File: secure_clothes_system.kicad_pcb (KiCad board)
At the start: 2 copper layers, 0 parts

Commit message: Made the first version of the layout with the ESP32-C3
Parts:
- added AE1: PCB_Antenna_Shield, RF_Antenna:PCB_ANTENNA_2,4GHz_50Ohm, F.Cu at (146.9, 76.0)
- added BT1: Battery_Cell, Connector_PinHeader_2.00mm:PinHeader_1x02_P2.00mm_Vertical, F.Cu at (156.0, 100.5)
- added C1: 4.7uF, Capacitor_SMD:C_0603_1608Metric, F.Cu at (152.7, 102.2)
- added C10: 0.1uF, Capacitor_SMD:C_0402_1005Metric, F.Cu at (151.5, 81.9)
- added C11: 10uF, Capacitor_SMD:C_0805_2012Metric, F.Cu at (143.7, 81.8)
- added C12: 0.1uF, Capacitor_SMD:C_0402_1005Metric, F.Cu at (144.8, 83.8)
- added C13: 1uF, Capacitor_SMD:C_0603_1608Metric, F.Cu at (146.9, 84.1)
- added C14: 1uF, Capacitor_SMD:C_0603_1608Metric, F.Cu at (142.9, 100.0)
- added C15: 1uF, Capacitor_SMD:C_0603_1608Metric, B.Cu at (152.7, 91.5)
- added C16: 1uF, Capacitor_SMD:C_0603_1608Metric, F.Cu at (142.9, 90.2)
- added C2: 10uF, Capacitor_SMD:C_0805_2012Metric, F.Cu at (151.9, 96.5)
- added C3: 1.5pF, Capacitor_SMD:C_0201_0603Metric, F.Cu at (147.1, 81.2)
- added C4: 6pF, Capacitor_SMD:C_0603_1608Metric, F.Cu at (159.2, 83.0)
- added C5: 6pF, Capacitor_SMD:C_0603_1608Metric, F.Cu at (155.2, 78.9)
- added C6: 1.5pF, Capacitor_SMD:C_0201_0603Metric, F.Cu at (149.3, 82.4)
- added C7: 1uF, Capacitor_SMD:C_0603_1608Metric, F.Cu at (153.2, 91.5)
- added C8: 10nF, Capacitor_SMD:C_0603_1608Metric, F.Cu at (146.7, 89.9)
- added C9: 0.1uF, Capacitor_SMD:C_0402_1005Metric, F.Cu at (151.5, 80.9)
- added J1: UART0, Connector_PinHeader_2.00mm:PinHeader_1x04_P2.00mm_Vertical, F.Cu at (163.1, 85.9)
- added L1: 2.2uH, Inductor_SMD:L_Murata_DFE201610P, F.Cu at (149.0, 96.4)
- added L2: 2.5nH, Inductor_SMD:L_0201_0603Metric, F.Cu at (148.2, 81.8)
- added L3: 2nH, Inductor_SMD:L_0201_0603Metric, F.Cu at (146.5, 82.9)
- added R1: 267K, Resistor_SMD:R_0603_1608Metric, F.Cu at (149.7, 102.2)
- added R2: 22, Resistor_SMD:R_0603_1608Metric, F.Cu at (154.1, 82.5)
- added R3: 10k, Resistor_SMD:R_0603_1608Metric, F.Cu at (142.9, 97.0)
- added R4: 10k, Resistor_SMD:R_0603_1608Metric, F.Cu at (142.9, 87.2)
- added SW1: BOOT, Button_Switch_THT:SW_PUSH_1P1T_6x3.5mm_H5.0_APEM_MJTP1250, F.Cu at (140.1, 95.3)
- added SW2: RST, Button_Switch_THT:SW_PUSH_1P1T_6x3.5mm_H5.0_APEM_MJTP1250, F.Cu at (140.1, 85.5)
- added U1: TPS62842DGRR, Package_SO:HVSSOP-8-1EP_3x3mm_P0.65mm_EP1.57x1.89mm_ThermalVias, F.Cu at (151.1, 99.6)
- added U2: ESP32-C3, Package_DFN_QFN:QFN-32-1EP_5x5mm_P0.5mm_EP3.45x3.45mm, F.Cu at (150.7, 87.0)
- added U3: W25X40CLSN, Package_SO:SOIC-8_3.9x4.9mm_P1.27mm, B.Cu at (157.2, 92.7)
- added Y1: 40MHz, Crystal:Crystal_SMD_3225-4Pin_3.2x2.5mm, F.Cu at (157.2, 80.9)
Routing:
- net /ESP32-C3/BOOT: track 0.00 -> 16.4 mm
- net +3V3: track 0.00 -> 13.2 mm
- net /ESP32-C3/U0RXD: track 0.00 -> 12.5 mm
- net /ESP32-C3/U0TXD: track 0.00 -> 12.2 mm
- net /ESP32-C3/CHIP_EN: track 0.00 -> 11.7 mm
- net /ESP32-C3/XTAL_N: track 0.00 -> 10.3 mm
- net /ESP32-C3/VDD3P3: track 0.00 -> 4.93 mm
- net Net-(C5-Pad2): track 0.00 -> 3.53 mm
- net /ESP32-C3/XTAL_P: track 0.00 -> 2.24 mm
- added copper zone on F.Cu, net GND
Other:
- board outline added: 28 x 33.9 mm
- copper layers 2 -> 4

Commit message: Made some fixes with the layout
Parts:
- C1, C13, C14, C15, C16, C4, C5, C7, C8: footprint Capacitor_SMD:C_0603_1608Metric -> Capacitor_SMD:C_0402_1005Metric
- C11, C2: footprint Capacitor_SMD:C_0805_2012Metric -> Capacitor_SMD:C_0402_1005Metric
- R1: value 267K -> 52.3K; footprint Resistor_SMD:R_0603_1608Metric -> Resistor_SMD:R_0402_1005Metric
- R2, R3, R4: footprint Resistor_SMD:R_0603_1608Metric -> Resistor_SMD:R_0402_1005Metric
- moved SW1 37.6 mm to (104.7, 108.0)
- moved SW2 37.6 mm to (104.7, 98.2)
- moved C8 30.4 mm to (176.7, 85.0), turned to 0 degrees
- moved C10 28.6 mm to (177.5, 93.9)
- moved C13 26.1 mm to (172.8, 86.8), turned to -90 degrees
- moved C11 26.1 mm to (169.3, 86.8), turned to -90 degrees
- moved C12 25.7 mm to (170.3, 86.8)
- moved L3 25.3 mm to (171.5, 86.3)
- moved C15 25.2 mm to (153.9, 116.6)
- moved U3 25.2 mm to (158.4, 117.8)
- moved U2 25.0 mm to (175.5, 90.0)
- moved C7 24.7 mm to (176.7, 84.0)
- moved C5 24.6 mm to (179.4, 82.7)
- moved R2 24.5 mm to (178.3, 86.1)
- moved AE1 24.4 mm to (170.9, 80.2)
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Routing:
- net +3V3: track 13.2 -> 30.6 mm, vias 0 -> 4
- net /ESP32-C3/BOOT: track 16.4 -> 0.00 mm
- net /ESP32-C3/U0RXD: track 12.5 -> 0.00 mm
- net /ESP32-C3/U0TXD: track 12.2 -> 0.00 mm
- net /ESP32-C3/CHIP_EN: track 11.7 -> 0.00 mm
- net /ESP32-C3/XTAL_N: track 10.3 -> 9.05 mm
- net /ESP32-C3/VDD3P3: track 4.93 -> 4.24 mm
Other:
- board size 28 x 33.9 mm -> 25.5 x 28.2 mm

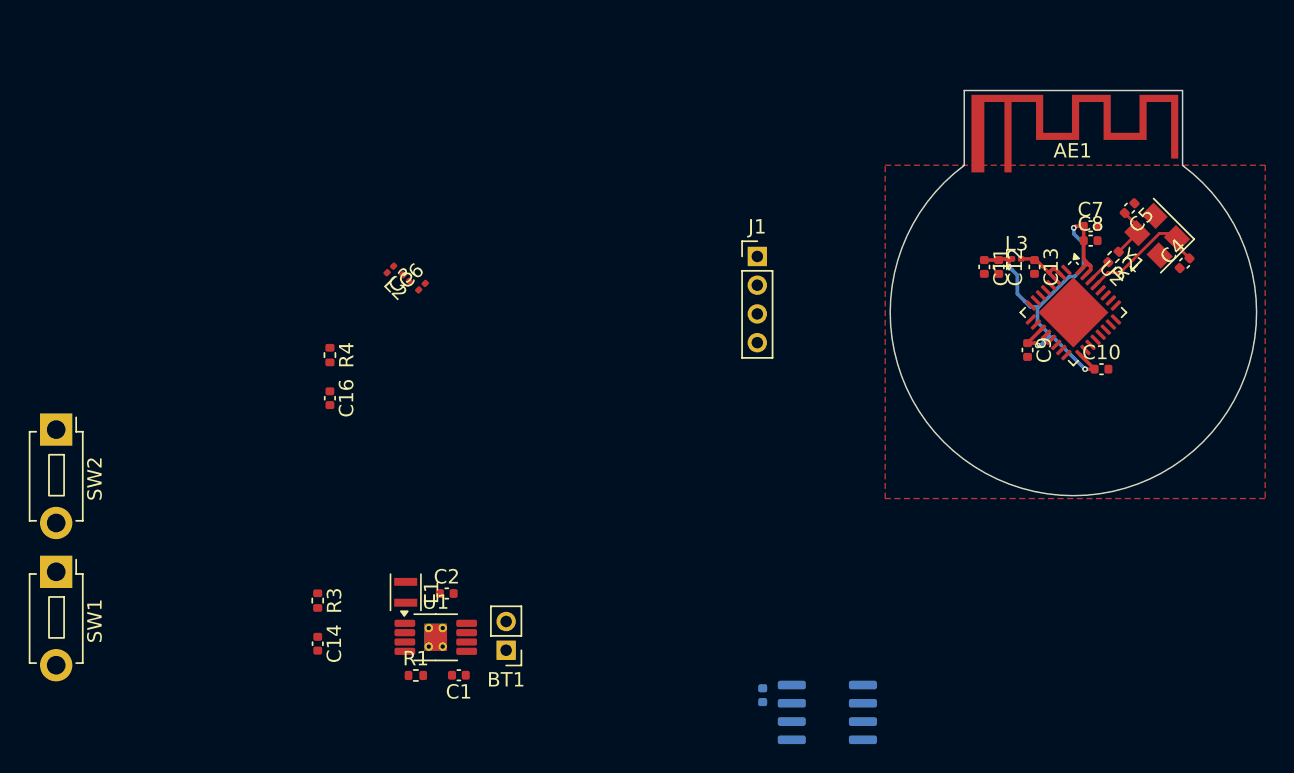
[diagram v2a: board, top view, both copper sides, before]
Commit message: Made the first version of the layout - DRC OK
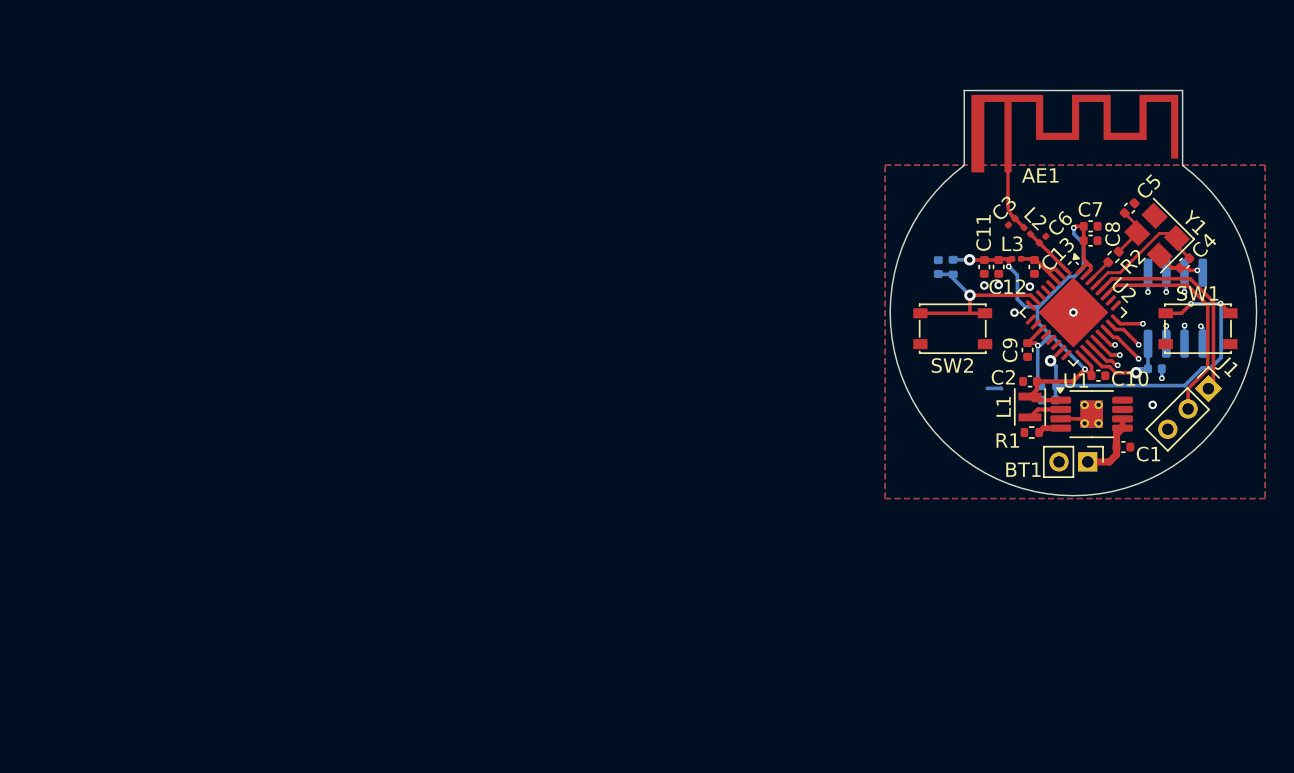
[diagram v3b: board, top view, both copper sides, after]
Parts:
- C14, C16, R3, R4: moved to B.Cu
- J1: footprint Connector_PinHeader_2.00mm:PinHeader_1x04_P2.00mm_Vertical -> Connector_PinHeader_2.00mm:PinHeader_1x03_P2.00mm_Vertical
- L2: value 2.5nH -> 2.6nH
- SW1, SW2: footprint Button_Switch_THT:SW_PUSH_1P1T_6x3.5mm_H5.0_APEM_MJTP1250 -> MSS_Devices:SW_SPST_PTS815
- moved SW1 81.3 mm to (184.2, 91.1), turned to 180 degrees
- moved SW2 62.8 mm to (167.1, 91.1), turned to 180 degrees
- moved C14 53.6 mm to (173.8, 96.1), turned to 180 degrees
- moved R3 53.0 mm to (173.8, 95.1), turned to 0 degrees
- moved C1 48.9 mm to (179.0, 99.4), turned to 0 degrees
- moved U1 48.2 mm to (176.8, 97.1)
- moved R1 46.1 mm to (172.6, 98.4), turned to 180 degrees
- moved L1 45.3 mm to (172.5, 96.6), turned to 90 degrees
- moved R4 43.8 mm to (167.1, 86.8)
- moved C3 43.4 mm to (171.2, 83.7)
- moved L2 43.4 mm to (172.3, 84.3), turned to -45 degrees
- moved C16 43.3 mm to (166.1, 86.8), turned to 90 degrees
- moved C6 43.3 mm to (173.4, 84.9)
- moved C2 43.2 mm to (172.5, 94.8), turned to 180 degrees
- moved BT1 42.6 mm to (176.5, 100.4), turned to -90 degrees
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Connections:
- J1 pad 1: +3V3 -> /ESP32-C3/U0TXD
- J1 pad 2: /ESP32-C3/U0TXD -> /ESP32-C3/U0RXD
- J1 pad 3: /ESP32-C3/U0RXD -> GND
- SW1 pad 2: /ESP32-C3/BOOT -> GND
- SW2 pad 2: /ESP32-C3/CHIP_EN -> GND
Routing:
- net /ESP32-C3/BOOT: track 0.00 -> 25.1 mm, vias 0 -> 3
- net /ESP32-C3/U0RXD: track 0.00 -> 15.7 mm
- net /ESP32-C3/U0TXD: track 0.00 -> 15.0 mm
- net /ESP32-C3/CHIP_EN: track 0.00 -> 13.5 mm, vias 0 -> 1
- net +3V3: track 30.6 -> 43.4 mm, vias 4 -> 5
- net /ESP32-C3/SPIWP: track 0.00 -> 10.2 mm, vias 0 -> 2
- net /ESP32-C3/SPID: track 0.00 -> 9.58 mm, vias 0 -> 2
- net /ESP32-C3/SPICLK: track 0.00 -> 8.90 mm, vias 0 -> 2
- net /ESP32-C3/SPIHD: track 0.00 -> 8.81 mm, vias 0 -> 2
- net /ESP32-C3/SPICS0: track 0.00 -> 7.28 mm, vias 0 -> 2
- net /ESP32-C3/VDD_SPI: track 0.00 -> 6.87 mm, vias 0 -> 1
- net GND: track 0.00 -> 6.52 mm, vias 0 -> 8
- net /ESP32-C3/SPIQ: track 0.00 -> 6.30 mm, vias 0 -> 2
- net /BATT: track 0.00 -> 4.88 mm
- net Net-(AE1-A): track 0.00 -> 4.63 mm
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- added copper zone on B.Cu, net GND
- added copper zone on In1.Cu, net GND

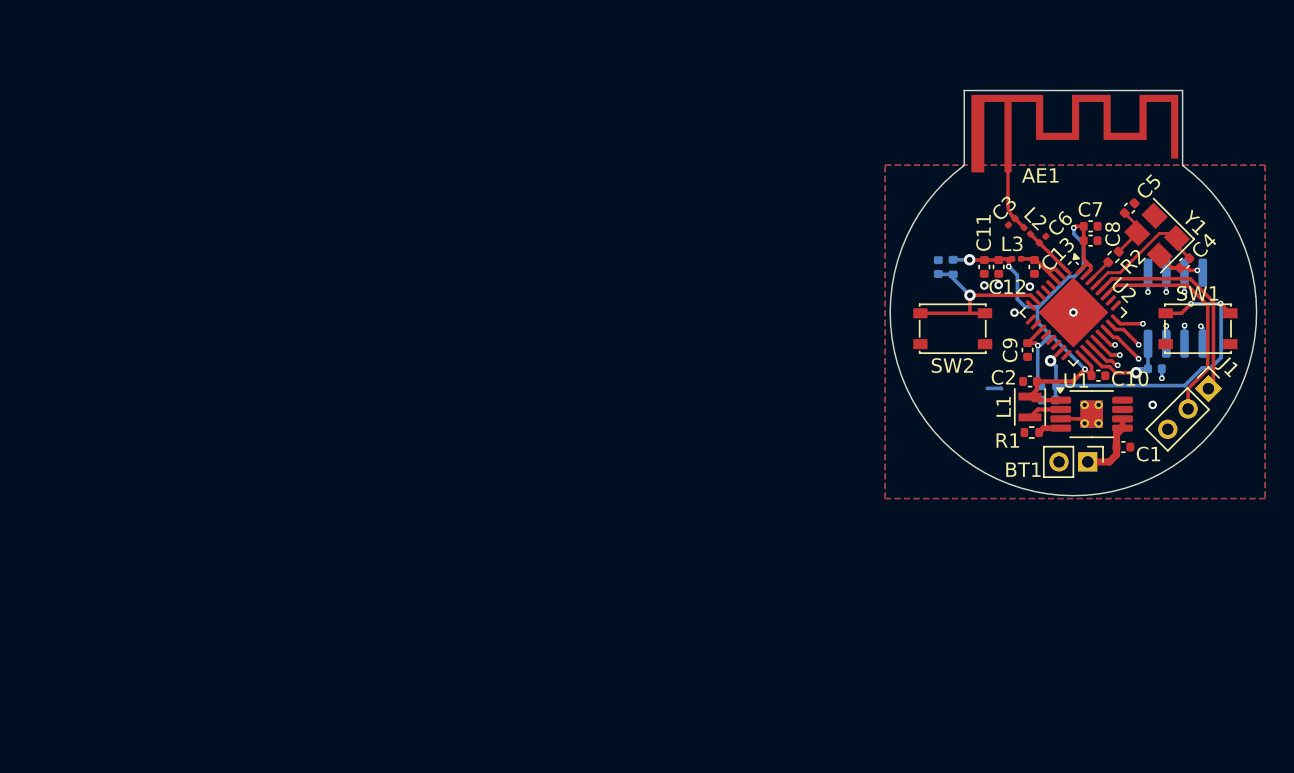
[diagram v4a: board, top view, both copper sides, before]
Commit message: Solved some warnings
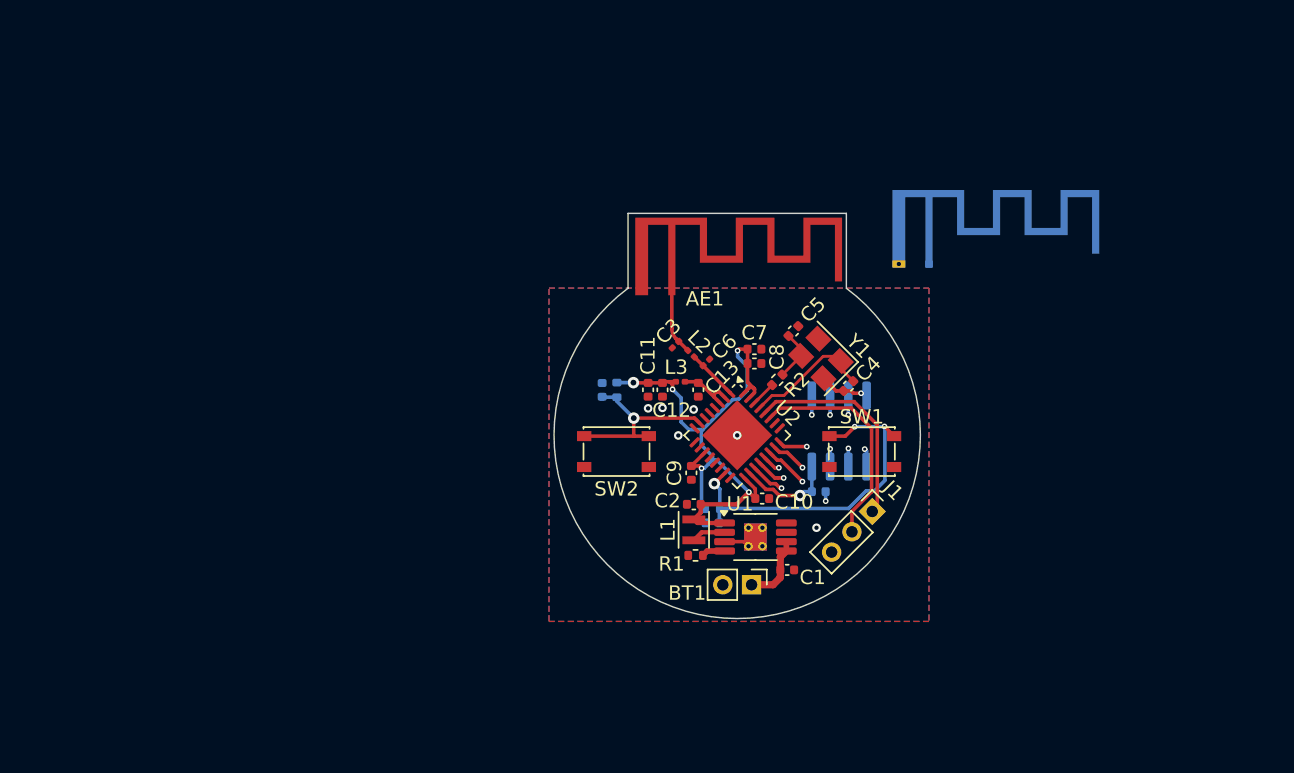
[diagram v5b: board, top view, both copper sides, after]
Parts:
- removed the AE1 at (170.9, 80.2)
- added AE1: PCB_Antenna_Shield, RF_Antenna:PCB_ANTENNA_2,4GHz_50Ohm, F.Cu at (147.6, 88.8)
- added AE1: PCB_Antenna_Shield, RF_Antenna:Texas_SWRA117D_2.4GHz_Left, B.Cu at (165.4, 86.6)
- moved C4 24.9 mm to (159.8, 95.1)
- moved C5 24.9 mm to (156.0, 91.3)
- moved R2 24.9 mm to (154.9, 94.7)
- moved SW2 24.9 mm to (143.7, 99.7)
- moved BT1 24.9 mm to (153.1, 109.0)
- moved C10 24.9 mm to (153.8, 103.0)
- moved C11 24.9 mm to (145.9, 95.4)
- moved C12 24.9 mm to (146.9, 95.4)
- moved C13 24.9 mm to (149.4, 95.4)
- moved C14 24.9 mm to (150.4, 104.6)
- moved C15 24.9 mm to (157.8, 102.5)
- moved C16 24.9 mm to (142.7, 95.4)
- moved C2 24.9 mm to (149.1, 103.3)
- moved C3 24.9 mm to (147.8, 92.2)
- moved C6 24.9 mm to (150.0, 93.5)
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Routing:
- net GND: track 6.52 -> 5.51 mm

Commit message: Fabrication.kicad_jobset added.
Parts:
- removed the AE1 at (165.4, 86.6)
- AE1: footprint RF_Antenna:PCB_ANTENNA_2,4GHz_50Ohm -> RF_Antenna:Texas_SWRA117D_2.4GHz_Left
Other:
- board text added: "0"
- board text added: "0 mm"
- board text added: "0.01016 mm"
- board text added: "0.011735 mm"
- board text added: "0.02"
- board text added: "0.034798 mm"
- board text added: "0.1000 mm / 0.1000 mm"
- board text added: "0.2000 mm"
- board text added: "0.2032 mm"
- board text added: "0.3048 mm"
- board text added: "0.8246 mm"
- board text added: "1"
- board text added: "25.5049 mm x 28.2026 mm"
- board text added: "3.3"
- board text added: "4"
- board text added: "4.39"
- board text added: "4.43"
- board text added: "B.Cu"
- board text added: "B.Mask"
- board text added: "B.Paste"
- board text added: "B.Silkscreen"
- board text added: "BOARD CHARACTERISTICS"
- board text added: "Board Thickness:"
- board text added: "Board overall dimensions:"
- board text added: "Bottom Silk Screen"
- board text added: "Bottom Solder Mask"
- board text added: "Bottom Solder Paste"
- board text added: "Castellated pads:"
- board text added: "Color"
- board text added: "Copper Finish:"
- board text added: "Copper Layer Count:"
- board text added: "Dielectric"
- board text added: "Edge card connectors:"
- board text added: "Epsilon R"
- board text added: "F.Cu"
- board text added: "F.Mask"
- board text added: "F.Paste"
- board text added: "F.Silkscreen"
- board text added: "FR4"
- board text added: "Impedance Control:"
- board text added: "In1.Cu"
- board text added: "In2.Cu"
- board text added: "Layer Name"
- board text added: "Loss Tangent"
- board text added: "Material"
- board text added: "Min hole diameter:"
- board text added: "Min track/spacing:"
- board text added: "No"
- board text added: "None"
- board text added: "Not specified"
- board text added: "Plated Board Edge:"
- board text added: "Thickness (mm)"
- board text added: "Top Silk Screen"
- board text added: "Top Solder Mask"
- board text added: "Top Solder Paste"
- board text added: "Type"
- board text added: "Yes"
- board text added: "copper"
- board text added: "core"
- board text added: "prepreg"
